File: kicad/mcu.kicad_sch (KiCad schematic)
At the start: 16 parts, among them U1 STM32WB55CEU6, Y1 32MHz, Y2 Crystal

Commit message: feat(schematic): add RF, SWD, and core MCU support circuitry
add unvalued capacitors for LSE crystal

add TDK_DLF162500LT-5028A1 symbol, footprint, and an unverified 3D model

add RF circuitry

add SWD circuitry

add BOOT0 circuitry

add NRST circuitry

add relevant notes for the newly added circuitry

modify net names and reference designators for HSE/LSE crystals
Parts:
- added C12, C13, C17: C, symbol Device:C
- added C14: 0p8, symbol Device:C
- added C15: 0p3, symbol Device:C
- added C16: 100n, symbol Device:C
- added FL1: TDK_DLF162500LT-5028A1, #odaij_RF_Filter:TDK_DLF162500LT-5028A1, symbol #odaij_RF_Filter:TDK_DLF162500LT-5028A1
- added J1: Conn_Coaxial, symbol Connector:Conn_Coaxial
- added J2: Conn_ARM_SWD_TagConnect_TC2030, Connector:Tag-Connect_TC2030-IDC-FP_2x03_P1.27mm_Vertical, symbol Connector:Conn_ARM_SWD_TagConnect_TC2030
- added L3: 2n7, symbol Device:L
- added R1, R2: R, symbol Device:R
- added SW1, SW2: SW_Push, symbol Switch:SW_Push
- X2: renamed from Y2; value Crystal -> 32kHz768
- renumbered Y1 to X1
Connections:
- net LSE_OSC_IN is gone; now on net LSE_IN: X2.1
- net +3V3: now also J2.1 (VCC), SW1.2
- net GND: now also C12.2, C13.2, C14.2, C15.2, C16.2, C17.2, FL1.2 (GND), FL1.4 (GND), J1.2 (Ext), J2.5 (GND), R1.2, SW2.1
- net RF: now reaches U1.21 (RF1)
- net RF: now also C14.1, L3.1
- net SWDIO: now reaches U1.39 (PA13)
- net SWDIO: now also J2.2 (SWDIO)
- net BOOT0: now reaches U1.4 (PH3)
- net BOOT0: now also C17.1, R1.1, R2.2
- net SWCLK: now reaches U1.41 (PA14)
- net SWCLK: now also J2.4 (SWCLK)
- net SWO: now reaches U1.43 (PB3)
- net SWO: now also J2.6 (SWO)
- net NRST: now reaches U1.7 (NRST)
- net NRST: now also C16.1, J2.3 (~{RESET}), SW2.2
- net HSE_OSC_IN renamed HSE_IN
- net HSE_OSC_OUT renamed HSE_OUT
- net LSE_OSC_ renamed LSE_IN
- net LSE_IN: now also C13.1; no longer U1.3 (PC15)
- net LSE_OSC_OUT renamed LSE_OUT
- net LSE_OUT: now also U1.3 (PC15), C12.1
- net VFBSMPS renamed SMPSFB
- net VLLSMPS renamed SMPSLXL
- net VLXSMPS renamed SMPSLX
- new net: R2.1, SW1.1
- new net RF_ANT: FL1.3 (OUT), J1.1 (In)
- new net RF_MATCH: C15.1, FL1.1 (IN), L3.2
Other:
- note added: "50 Ohms Matching Network"
- note added: "External Reset Circuit"
- note added: "For any connector or exposed interface you typically should add ESD protection to make sure when you're messing around with the board you don't accidentally fry your devices. However, phil says that from his experience these ST mcus are pretty resilient, so it's fine for *test boards* to skip them, however he doesn't recommend this for connectors on commercial boards"
- note added: "HSE - 32MHz"
- note added: "Miscellaneous"
- note added: "QUESTION what is IN/OUT? check app. note"
- note added: "RF"
- note added: "Serial Wire Debug"
- note added: "phil doesn't typically use the switch because he does that using the debugger however, he does place the capacitor as per the datasheet. for me, I'll keep the switch."
- note added: "run mode by default. bootloader when pressed"
- note added: "switch can be used as a user switch after boot"
- note added: "todo: 10k ohms maybe?"
- note added: "todo: LPF values (debouncing circuit)"
- note removed: "HSE - 32MHz TODO verify"
- note removed: "TODO check which is OUT/IN"
- moved on the sheet: C11, L1, L2

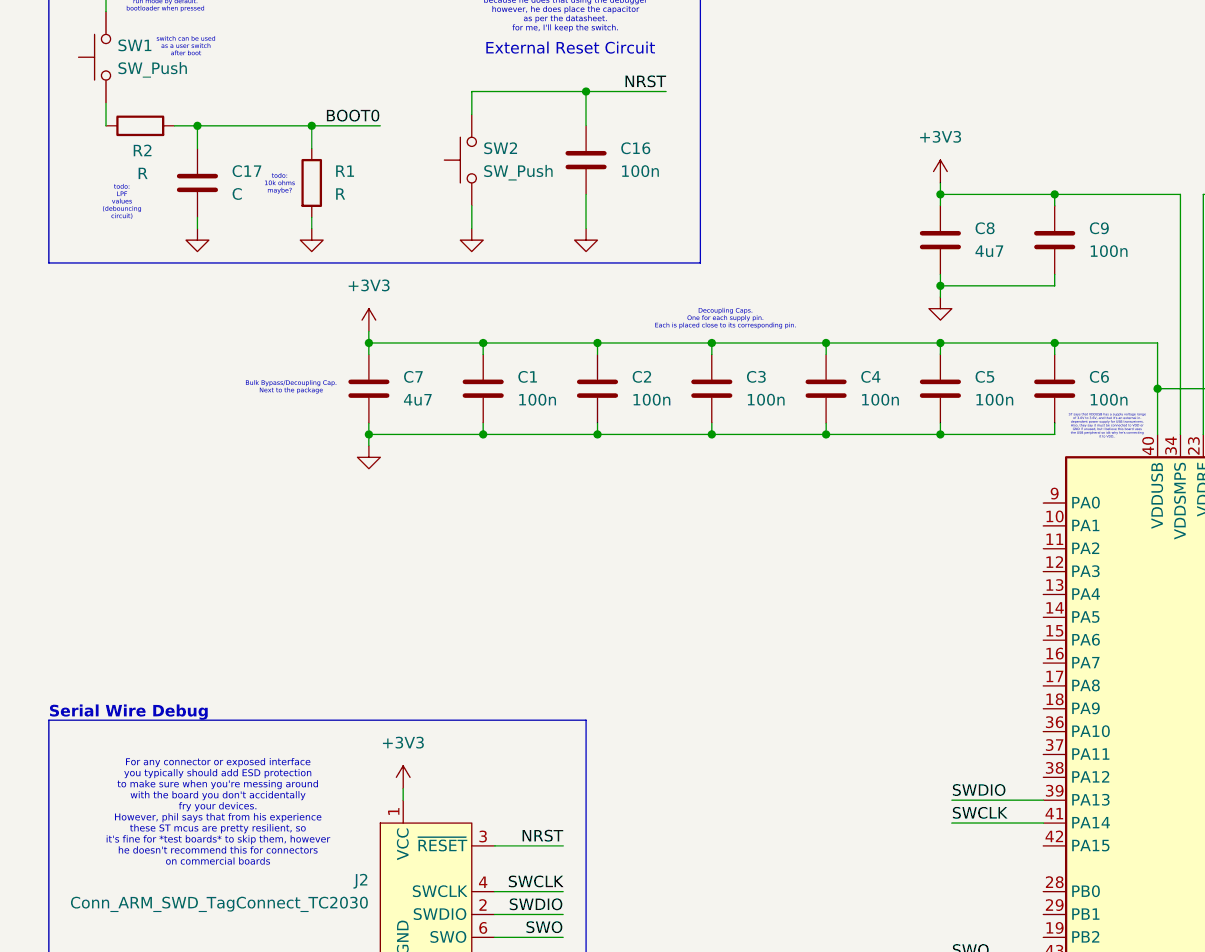
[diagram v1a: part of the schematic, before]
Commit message: feat (schematic): add basmala to root, create new hierarchical sheet for usb inside root, and more /stm32-bt-board/ add basmala to root schematic - add a new usb hierarchical sheet to root
/stm32-bt-board/Microcontroller/
- add resistance value for BOOT0 LPF

/stm32-bt-board/USB/
- add usb type c receptacle
- add the usblc6-2sc6 protection ic to D- and D+
- add 5k1 pull down resistors for CC1 and CC2
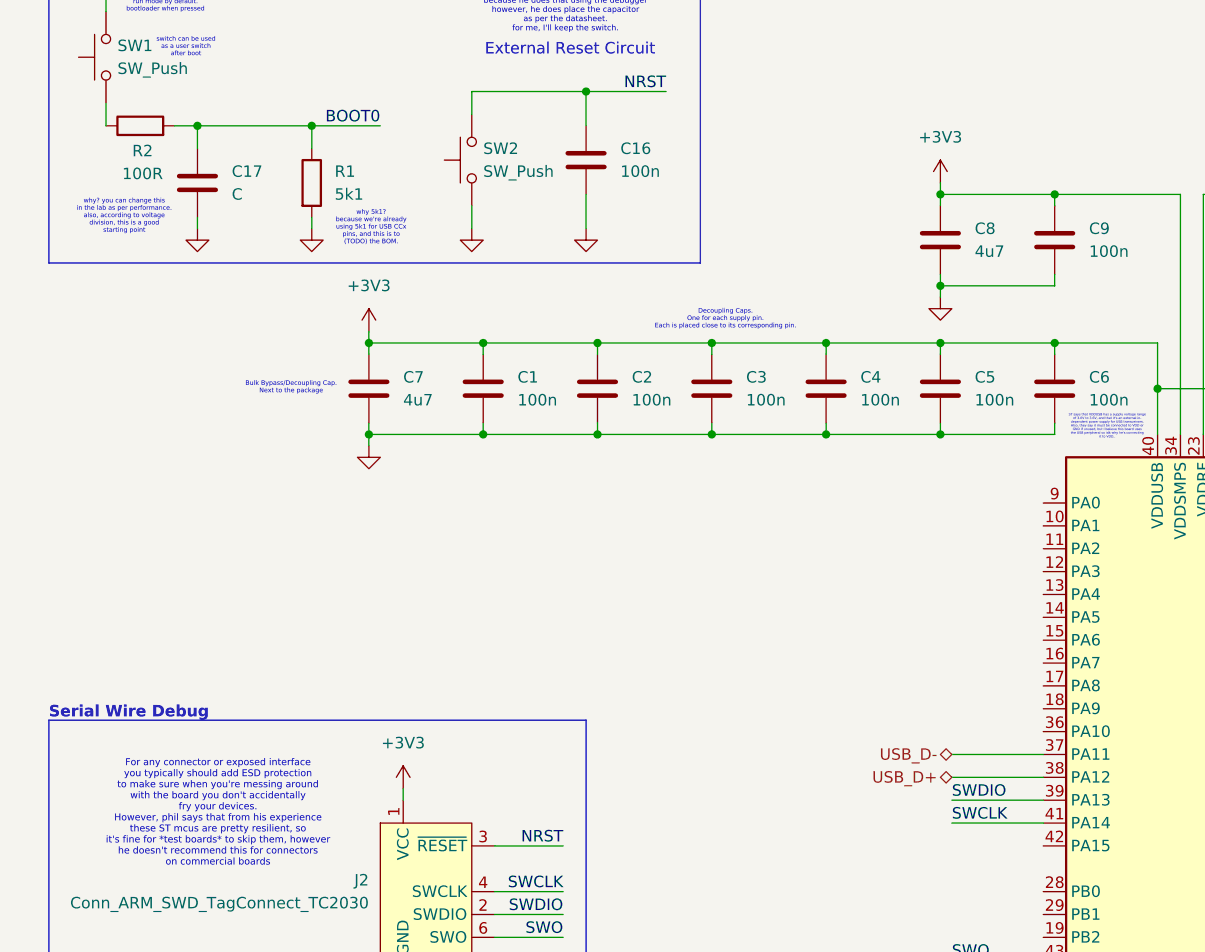
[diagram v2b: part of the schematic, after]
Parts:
- R1: value R -> 5k1
- R2: value R -> 100R
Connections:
- net USB_D-: now reaches U1.37 (PA11)
- net USB_D+: now reaches U1.38 (PA12)
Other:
- note added: "why 5k1? because we're already using 5k1 for USB CCx pins, and this is to (TODO) the BOM."
- note added: "why? you can change this in the lab as per performance. also, according to voltage division, this is a good starting point"
- note removed: "todo: 10k ohms maybe?"
- note removed: "todo: LPF values (debouncing circuit)"
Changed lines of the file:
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@@
 		)
 	)
-	(text "todo:\n10k ohms\nmaybe?"
+	(text "why 5k1?\nbecause we're already\nusing 5k1 for USB CCx\npins, and this is to\n(TODO) the BOM."
 		(exclude_from_sim no)
-		(at 43.434 47.244 0)
+		(at 53.594 52.07 0)
 		(effects
 			(font
@@
 		)
 	)
-	(text "todo:\nLPF\nvalues\n(debouncing\ncircuit)"
+	(text "why? you can change this\nin the lab as per performance.\nalso, according to voltage\ndivision, this is a good\nstarting point"
 		(exclude_from_sim no)
-		(at 25.908 49.276 0)
+		(at 26.162 50.8 0)
 		(effects
 			(font
@@
 	(wire
 		(pts
+			(xy 118.11 110.49) (xy 128.27 110.49)
+		)
+		(stroke
+			(width 0)
+			(type default)
+		)
+	)
+	(wire
+		(pts
 			(xy 46.99 40.64) (xy 54.61 40.64)
 		)
@@
 	(wire
 		(pts
+			(xy 118.11 113.03) (xy 128.27 113.03)
+		)
+		(stroke
+			(width 0)
+			(type default)
+		)
+	)
+	(wire
+		(pts
 			(xy 140.97 69.85) (xy 140.97 74.93)
 		)
@@
 		)
 	)
+	(hierarchical_label "USB_D+"
+		(shape bidirectional)
+		(at 118.11 113.03 180)
+		(effects
+			(font
+				(size 1.27 1.27)
+			)
+			(justify right)
+		)
+	)
+	(hierarchical_label "USB_D-"
+		(shape bidirectional)
+		(at 118.11 110.49 180)
+		(effects
+			(font
+				(size 1.27 1.27)
+			)
+			(justify right)
+		)
+	)
 	(symbol
 		(lib_id "#odaij_RF_Filter:TDK_DLF162500LT-5028A1")
@@
 			)
 		)
-		(property "Value" "R"
+		(property "Value" "5k1"
 			(at 49.53 48.2599 0)
 			(show_name no)
@@
 			)
 		)
-		(property "Value" "R"
+		(property "Value" "100R"
 			(at 28.194 45.974 90)
 			(show_name no)

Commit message: A LOT OF STUFF
I almost finished the schematic part of the tutorial
what remains is part choosing and filling the relevant fields for every component
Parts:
- removed C1, C10, C16, C2, C3, C4, C5, C6, C9: 100n, symbol Device:C
- removed C11, C7, C8: 4u7, symbol Device:C
- removed C12, C13, C17: C, symbol Device:C
- removed C14: 0p8, symbol Device:C
- removed C15: 0p3, symbol Device:C
- removed FL1: TDK_DLF162500LT-5028A1, #odaij_RF_Filter:TDK_DLF162500LT-5028A1, symbol #odaij_RF_Filter:TDK_DLF162500LT-5028A1
- removed J1: Conn_Coaxial, symbol Connector:Conn_Coaxial
- removed J2: Conn_ARM_SWD_TagConnect_TC2030, Connector:Tag-Connect_TC2030-IDC-FP_2x03_P1.27mm_Vertical, symbol Connector:Conn_ARM_SWD_TagConnect_TC2030
- removed L1: 10n, symbol Device:L
- removed L2: 10u, symbol Device:L
- removed L3: 2n7, symbol Device:L
- removed R1: 5k1, symbol Device:R
- removed R2: 100R, symbol Device:R
- removed SW1, SW2: SW_Push, symbol Switch:SW_Push
- removed X1: 32MHz, symbol Device:Crystal_GND24
- removed X2: 32kHz768, symbol Device:Crystal
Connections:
- net UART_TX: now reaches U1.11 (PA2)
- net UART_RX: now reaches U1.12 (PA3)
- net USER_LED: now reaches U1.16 (PA7)
- net HSE_IN renamed OSC_IN
- net HSE_OUT renamed OSC_OUT
- net LSE_IN renamed OSC_LSE_IN
- net LSE_OUT renamed OSC_LSE_OUT
- no-connect marks 0 -> 19
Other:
- added sheet Crystals (mcu_crystals.kicad_sch)
- added sheet Decoupling Capacitors (mcu_decoupling_capacitors.kicad_sch)
- added sheet Micellaneous (mcu_miscellaneous.kicad_sch)
- added sheet RF Front End (mcu_rf.kicad_sch)
- added sheet SMPS (mcu_smps.kicad_sch)
- note removed: "50 Ohms Matching Network"
- note removed: "Bulk Bypass/Decoupling Cap. Next to the package"
- note removed: "Decoupling Caps. One for each supply pin. Each is placed close to its corresponding pin."
- note removed: "External Reset Circuit"
- note removed: "For any connector or exposed interface you typically should add ESD protection to make sure when you're messing around with the board you don't accidentally fry your devices. However, phil says that from his experience these ST mcus are pretty resilient, so it's fine for *test boards* to skip them, however he doesn't recommend this for connectors on commercial boards"
- note removed: "HSE - 32MHz"
- note removed: "HSE/LSE Crystals"
- note removed: "LSE - 32KHz768"
- note removed: "Miscellaneous"
- note removed: "QUESTION what is IN/OUT? check app. note"
- note removed: "RF"
- note removed: "Reference board by ST has an extra 100pF cap in parallel, but phil explains this is not necessary since we're going to use modern packages that are small enough - such that we can place the 100nF cap close enough to the VDDRF pin. and that in this case the 100pF cap doesn't matter and doesn't add anything."
- note removed: "SMPS"
- note removed: "ST says that VDDUSB has a supply voltage range of 3.0V to 3.6V, and that it's an external in- dependent power supply for USB transceivers. Also, they say it must be connected to VDD or GND if unused, but I believe this board uses the USB peripheral so idk why he's connecting it to VDD.."
- note removed: "Serial Wire Debug"
- note removed: "TODO add capacitors"
- note removed: "https://www.st.com/resource/en/application_note/an2867-guidelines-for-oscillator-design-on-stm8afals-and-stm32-mcusmpus-stmicroelectronics.pdf"
- note removed: "https://www.st.com/resource/en/application_note/an5246-how-to-use-smps-to-improve-power-efficiency-on-stm32wb-mcus-stmicroelectronics.pdf"
- note removed: "phil also explains that paralelling DIFFERENT types of capacitors is typically not a good idea, and ty- pically not necessary. he also explains that it on- ly makes sense if the package sizes of the compone- nts are vastly different."
- note removed: "phil doesn't typically use the switch because he does that using the debugger however, he does place the capacitor as per the datasheet. for me, I'll keep the switch."
- note removed: "run mode by default. bootloader when pressed"
- note removed: "switch can be used as a user switch after boot"
- note removed: "why 5k1? because we're already using 5k1 for USB CCx pins, and this is to (TODO) the BOM."
- note removed: "why? you can change this in the lab as per performance. also, according to voltage division, this is a good starting point"

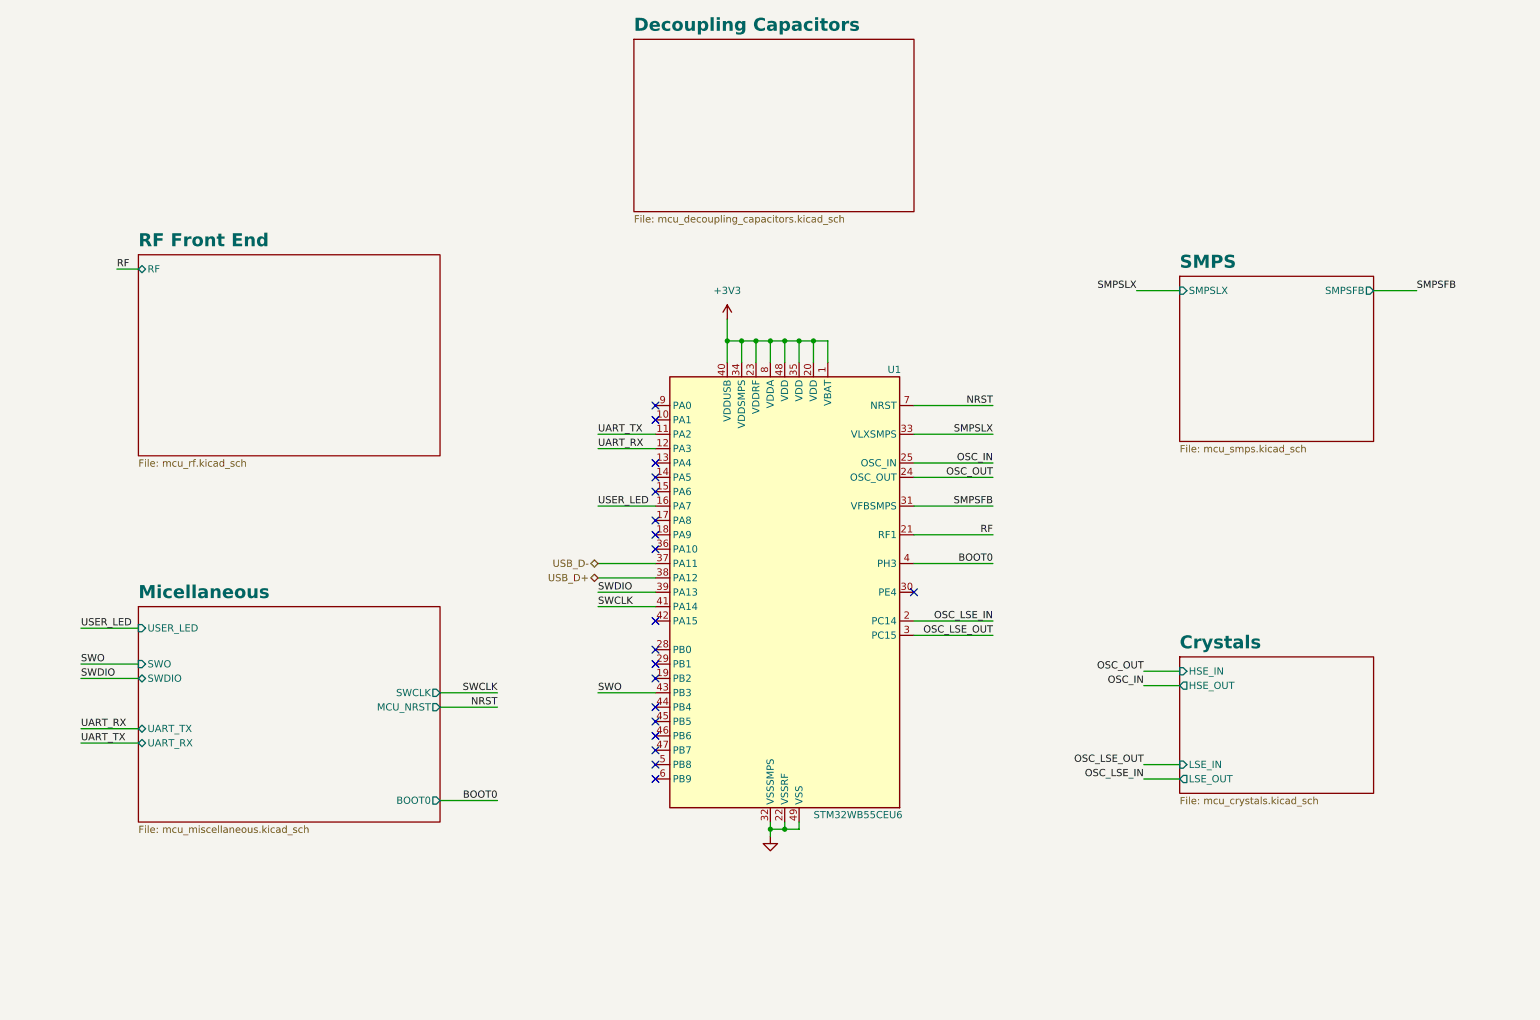
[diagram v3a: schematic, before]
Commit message: refactor(schematic): polish the schematic as much as possible - add new Basmala - fix netlist names almost EVERYWHERE, this is to help with net classes, and to help with building a good habit of naming nets properly - add a 100n capacitor to the SWD connector power pin - update many many other things EVERYWHERE
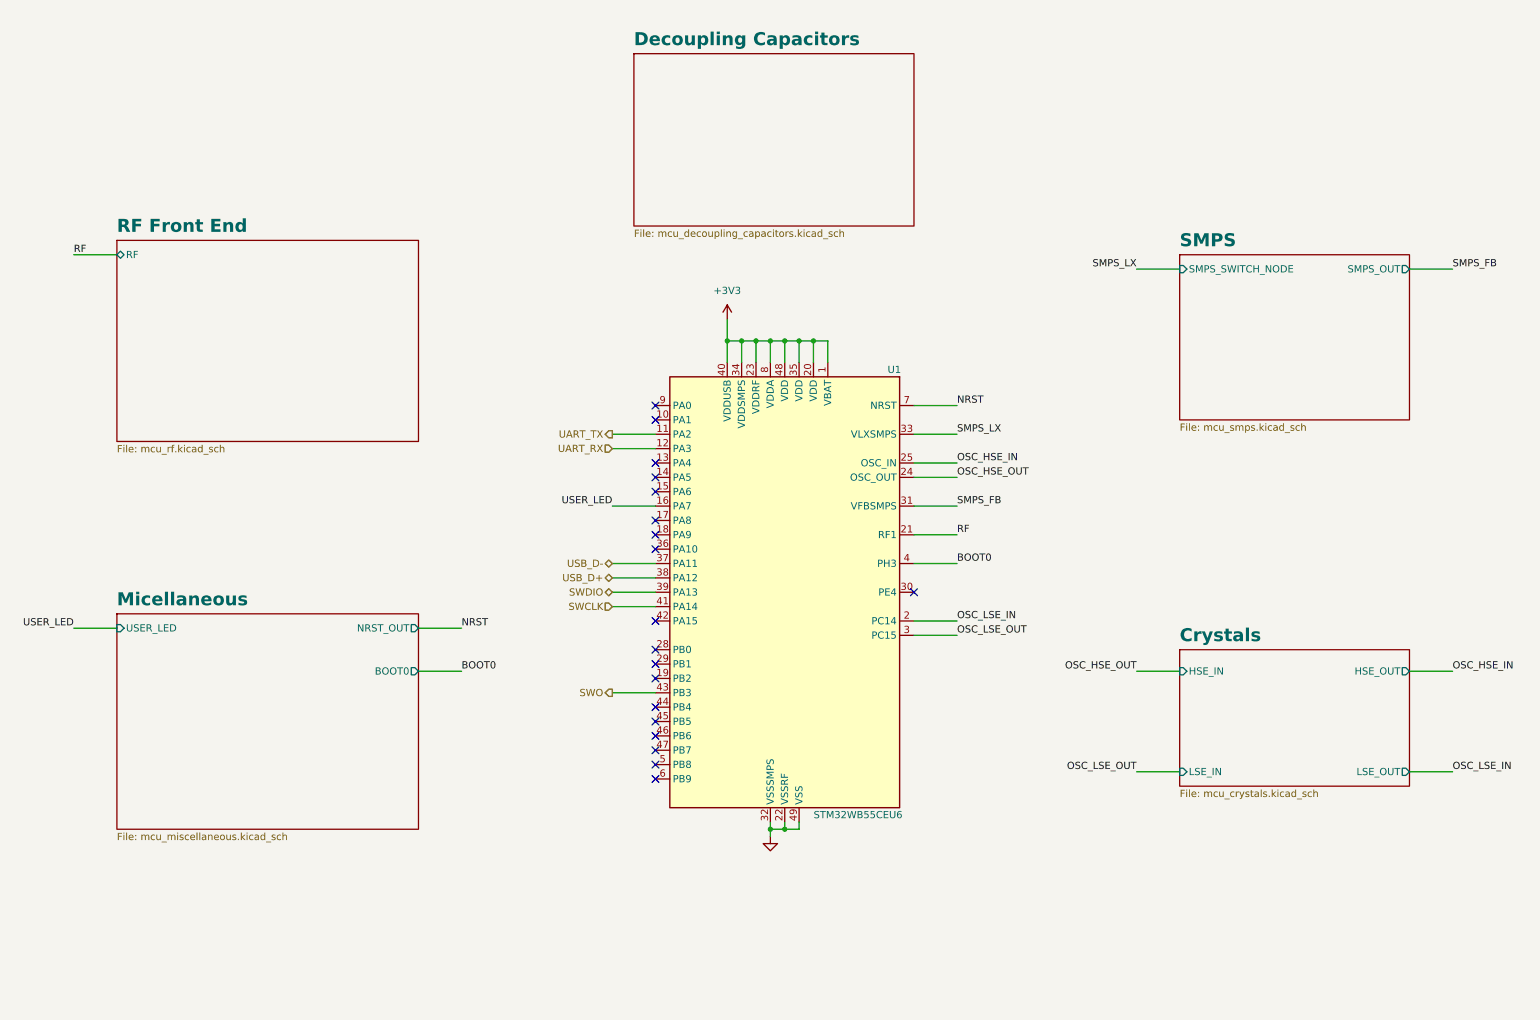
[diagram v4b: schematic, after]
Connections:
- net OSC_IN renamed OSC_HSE_IN
- net OSC_OUT renamed OSC_HSE_OUT
- net SMPSFB renamed SMPS_FB
- net SMPSLX renamed SMPS_LX
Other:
- sheet Micellaneous ports: added NRST_OUT; removed MCU_NRST, SWCLK, SWDIO, SWO, UART_RX, UART_TX
- sheet SMPS ports: added SMPS_OUT, SMPS_SWITCH_NODE; removed SMPSFB, SMPSLX
